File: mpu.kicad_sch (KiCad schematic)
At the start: 31 parts, among them SW501 SW_DIP_x03, U501 STM32MP135FAE7, Y501 32.768 kHz, Y502 24 MHz

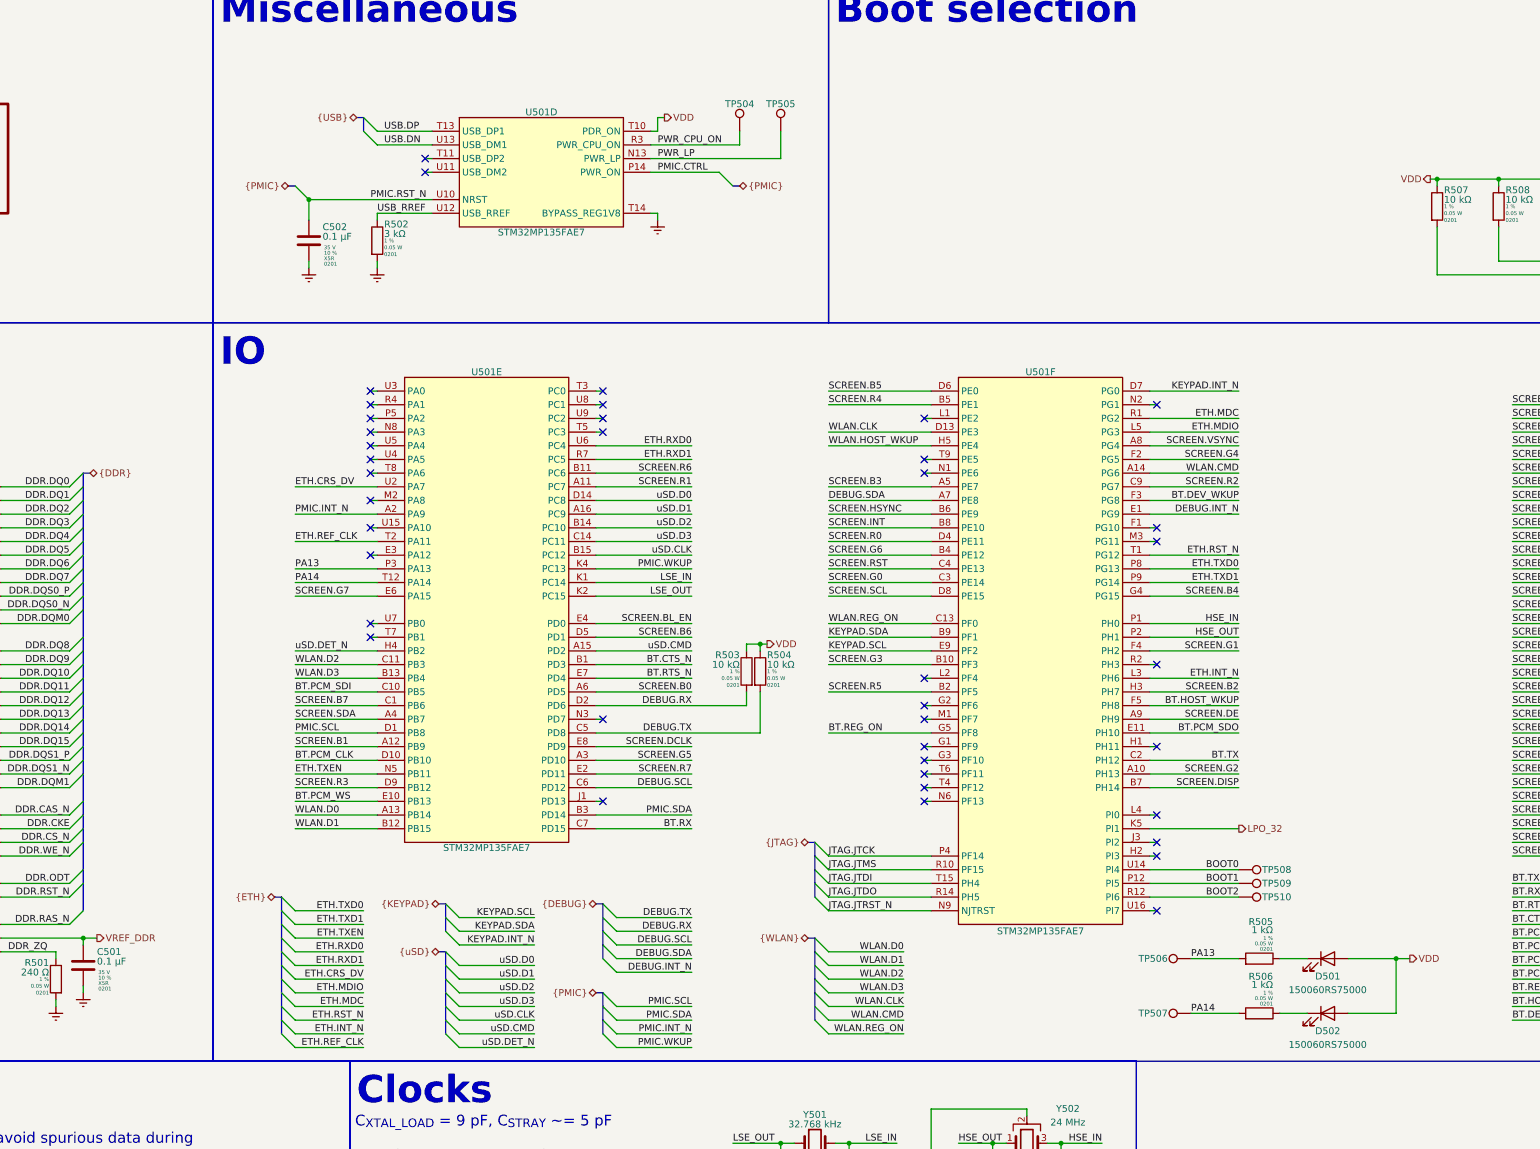
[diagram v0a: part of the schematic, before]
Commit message: Fix PMIC symbol and MPU labels
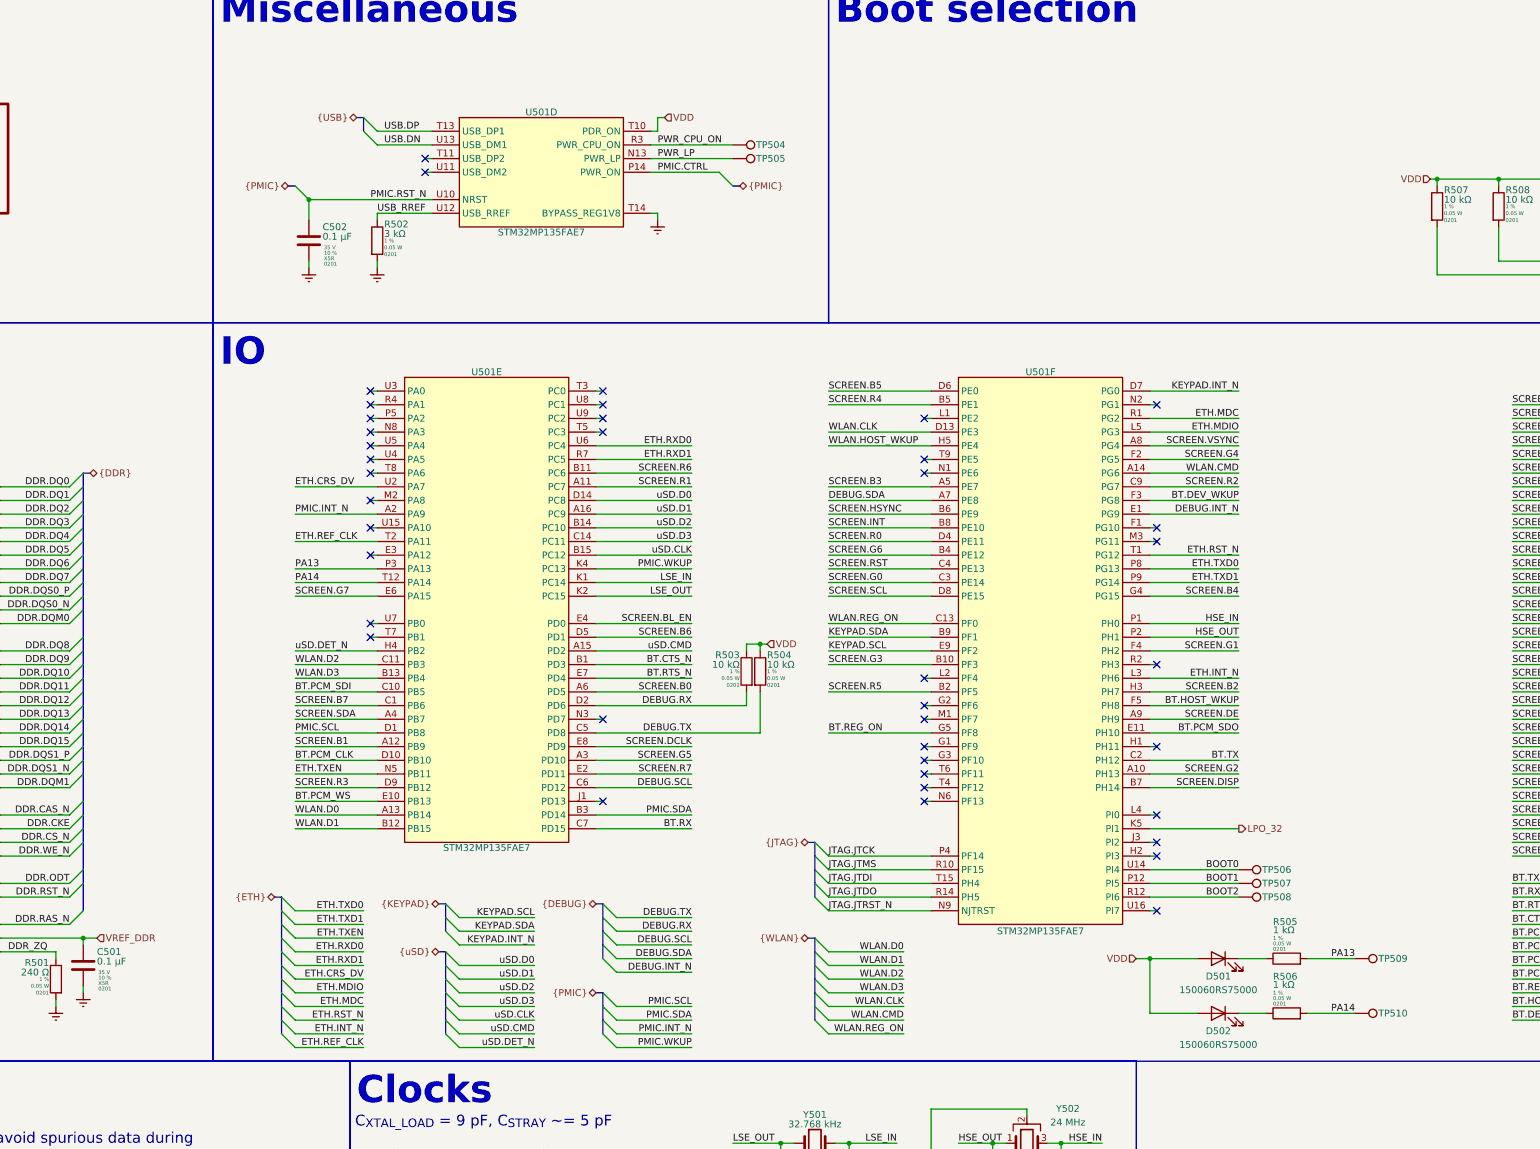
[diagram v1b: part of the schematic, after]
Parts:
- renumbered TP508 to TP506, TP509 to TP507, TP510 to TP508, TP506 to TP509, TP507 to TP510
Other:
- moved on the sheet: D501, D502, R505, R506, TP509, TP510

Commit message: Fix symbols and footprint assignments
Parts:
- SW501: footprint Package_DIP:DIP-6_W7.62mm -> Button_Switch_THT:SW_DIP_SPSTx03_Slide_9.78x9.8mm_W7.62mm_P2.54mm; symbol Switch:SW_DIP_x03 -> linux-sbc:SW_DIP_x03
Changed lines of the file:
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@@
 	)
 	(symbol
-		(lib_id "Switch:SW_DIP_x03")
+		(lib_id "linux-sbc:SW_DIP_x03")
 		(at 392.43 102.87 0)
 		(unit 1)
@@
 			)
 		)
-		(property "Footprint" "Package_DIP:DIP-6_W7.62mm"
+		(property "Footprint" "Button_Switch_THT:SW_DIP_SPSTx03_Slide_9.78x9.8mm_W7.62mm_P2.54mm"
 			(at 392.43 105.41 0)
 			(effects
@@
 			)
 		)
-		(property "Datasheet" "https://www.cuidevices.com/product/resource/ds01-254.pdf"
+		(property "Datasheet" "~"
 			(at 392.43 105.41 0)
 			(effects
@@
 			)
 		)
-		(property "Description" "Dip Switch SPST 3 Position Through Hole Slide (Standard) Actuator 25mA 24VDC"
+		(property "Description" "3x DIP Switch, Single Pole Single Throw (SPST) switch, small symbol"
 			(at 392.43 102.87 0)
 			(effects

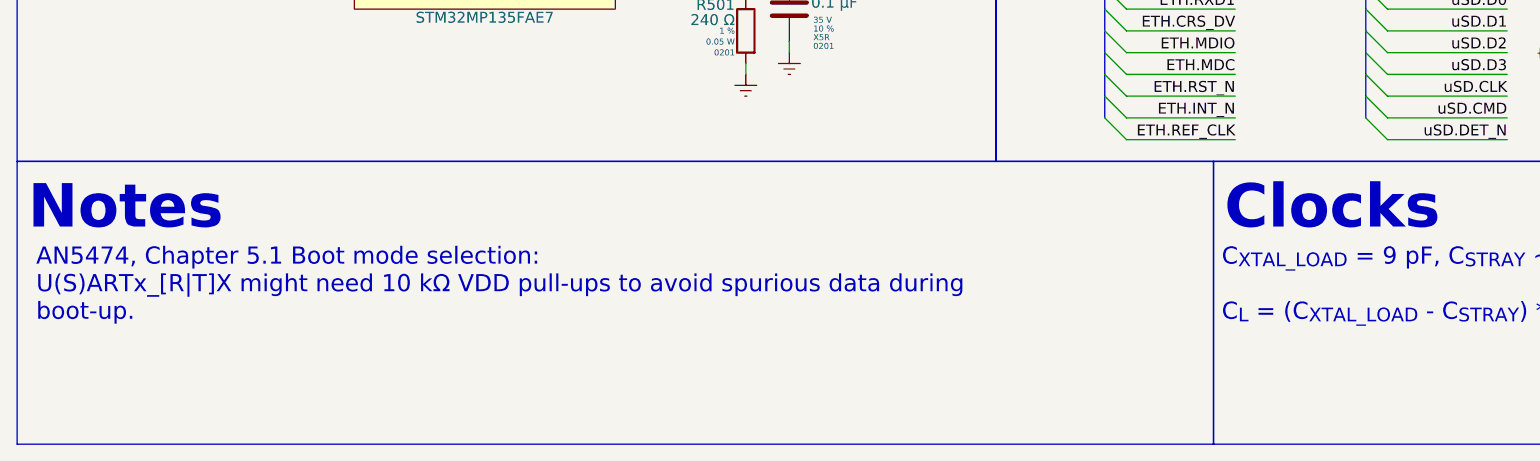
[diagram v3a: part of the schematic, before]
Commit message: Refactor text with ChatGPT and make schematics more readable
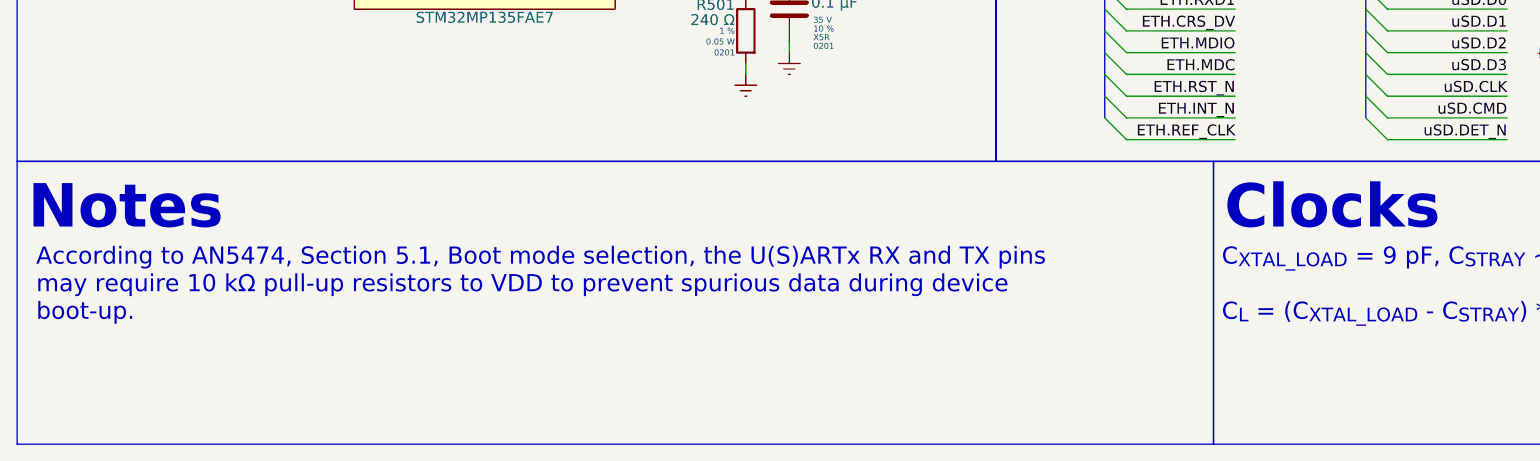
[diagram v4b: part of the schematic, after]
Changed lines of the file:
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@@
 		)
 	)
-	(text_box "AN5474, Chapter 5.1 Boot mode selection:\nU(S)ARTx_[R|T]X might need 10 kΩ VDD pull-ups to avoid spurious data during boot-up."
+	(text_box "According to AN5474, Section 5.1, Boot mode selection, the U(S)ARTx RX and TX pins may require 10 kΩ pull-up resistors to VDD to prevent spurious data during device boot-up."
 		(exclude_from_sim no)
 		(at 13.97 260.35 0)

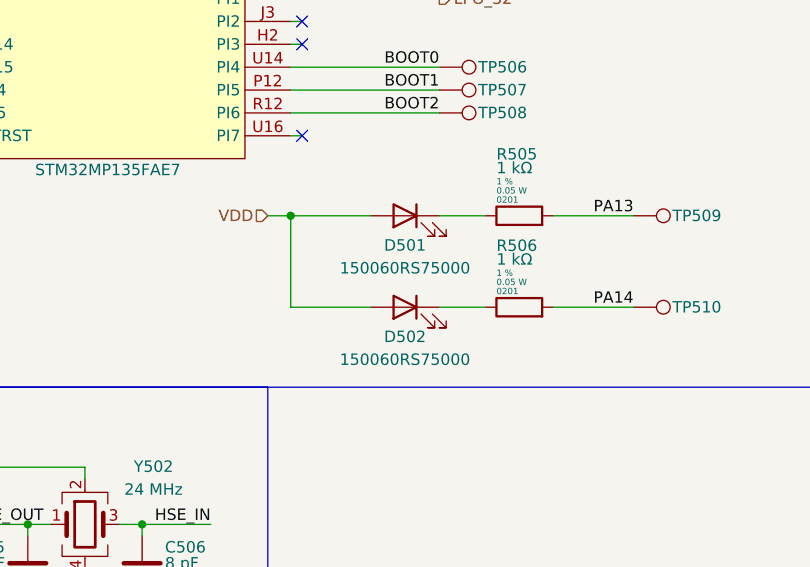
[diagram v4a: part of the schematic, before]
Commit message: Rework Red LED BOM and info, rework debug USB-to-UART
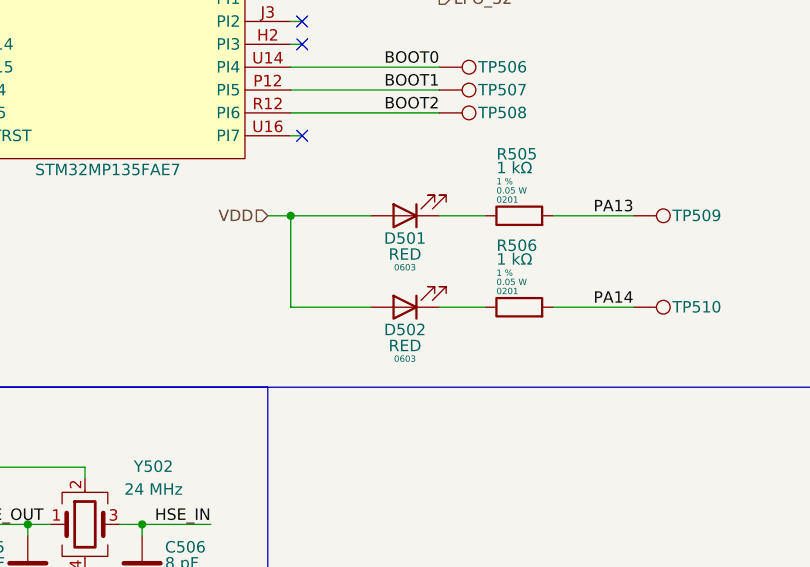
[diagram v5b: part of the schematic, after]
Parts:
- D501, D502: value 150060RS75000 -> RED; Size (none) -> 0603
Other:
- moved on the sheet: D501
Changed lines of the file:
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@@
 			)
 		)
-		(property "Datasheet" "~"
+		(property "Datasheet" "https://www.cuidevices.com/product/resource/ds01-254.pdf"
 			(at 392.43 105.41 0)
 			(effects
@@
 	)
 	(symbol
+		(lib_name "LED_1")
 		(lib_id "Device:LED")
-		(at 313.69 232.41 0)
-		(mirror y)
+		(at 313.69 232.41 180)
 		(unit 1)
 		(exclude_from_sim no)
@@
 		(dnp no)
 		(property "Reference" "D501"
-			(at 313.69 234.95 0)
+			(at 313.69 234.188 0)
 			(effects
 				(font
 					(size 1.27 1.27)
 				)
-				(justify top)
+				(justify bottom)
 			)
 		)
-		(property "Value" "150060RS75000"
-			(at 313.69 237.49 0)
+		(property "Value" "RED"
+			(at 313.69 235.966 0)
 			(effects
 				(font
 					(size 1.27 1.27)
 				)
-				(justify top)
+				(justify bottom)
 			)
 		)
@@
 			)
 		)
+		(property "Size" "0603"
+			(at 313.69 237.744 0)
+			(effects
+				(font
+					(size 0.7 0.7)
+				)
+				(justify bottom)
+			)
+		)
 		(pin "2"
 		)
@@
 	)
 	(symbol
-		(lib_id "Device:LED")
-		(at 313.69 242.57 0)
-		(mirror y)
-		(unit 1)
-		(exclude_from_sim no)
-		(in_bom yes)
-		(on_board yes)
-		(dnp no)
-		(property "Reference" "D502"
-			(at 313.69 245.11 0)
-			(effects
-				(font
-					(size 1.27 1.27)
-				)
-				(justify top)
-			)
-		)
-		(property "Value" "150060RS75000"
-			(at 313.69 247.65 0)
-			(effects
-				(font
-					(size 1.27 1.27)
-				)
-				(justify top)
-			)
-		)
-		(property "Footprint" "LED_SMD:LED_0603_1608Metric"
-			(at 313.69 242.57 0)
-			(effects
-				(font
-					(size 1.27 1.27)
-				)
-				(hide yes)
-			)
-		)
-		(property "Datasheet" "https://www.we-online.com/components/products/datasheet/150060RS75000.pdf"
-			(at 313.69 242.57 0)
-			(effects
-				(font
-					(size 1.27 1.27)
-				)
-				(hide yes)
-			)
-		)
-		(property "Description" "Red 625nm LED Indication - Discrete 2V 0603 (1608 Metric)"
-			(at 313.69 242.57 0)
-			(effects
-				(font
-					(size 1.27 1.27)
-				)
-				(hide yes)
-			)
-		)
-		(property "MPN" "150060RS75000"
-			(at 313.69 242.57 0)
-			(effects
-				(font
-					(size 1.27 1.27)
-				)
-				(hide yes)
-			)
-		)
-		(property "Manufacturer" "Würth Elektronik"
-			(at 313.69 242.57 0)
-			(effects
-				(font
-					(size 1.27 1.27)
-				)
-				(hide yes)
-			)
-		)
-		(property "Digi-Key Part Number" "732-4978-1-ND"
-			(at 313.69 242.57 0)
-			(effects
-				(font
-					(size 1.27 1.27)
-				)
-				(hide yes)
-			)
-		)
-		(pin "2"
-		)
-		(pin "1"
-		)
-		(instances
-			(project "linux-sbc"
-				(path "/fa11a02f-8043-4153-ab69-88d766503017/2d01087b-54dc-4f43-9cc7-a0ba17201776"
-					(reference "D502")
-					(unit 1)
-				)
-			)
-		)
-	)
-	(symbol
 		(lib_id "power:Earth")
 		(at 284.48 279.4 0)
@@
 					(unit 1)
 				)
+			)
+		)
+	)
+	(symbol
+		(lib_name "LED_1")
+		(lib_id "Device:LED")
+		(at 313.69 242.57 180)
+		(unit 1)
+		(exclude_from_sim no)
+		(in_bom yes)
+		(on_board yes)
+		(dnp no)
+		(property "Reference" "D502"
+			(at 313.69 244.348 0)
+			(effects
+				(font
+					(size 1.27 1.27)
+				)
+				(justify bottom)
+			)
+		)
+		(property "Value" "RED"
+			(at 313.69 246.126 0)
+			(effects
+				(font
+					(size 1.27 1.27)
+				)
+				(justify bottom)
+			)
+		)
+		(property "Footprint" "LED_SMD:LED_0603_1608Metric"
+			(at 313.69 242.57 0)
+			(effects
+				(font
+					(size 1.27 1.27)
+				)
+				(hide yes)
+			)
+		)
+		(property "Datasheet" "https://www.we-online.com/components/products/datasheet/150060RS75000.pdf"
+			(at 313.69 242.57 0)
+			(effects
+				(font
+					(size 1.27 1.27)
+				)
+				(hide yes)
+			)
+		)
+		(property "Description" "Red 625nm LED Indication - Discrete 2V 0603 (1608 Metric)"
+			(at 313.69 242.57 0)
+			(effects
+				(font
+					(size 1.27 1.27)
+				)
+				(hide yes)
+			)
+		)
+		(property "MPN" "150060RS75000"
+			(at 313.69 242.57 0)
+			(effects
+				(font
+					(size 1.27 1.27)
+				)
+				(hide yes)
+			)
+		)
+		(property "Manufacturer" "Würth Elektronik"
+			(at 313.69 242.57 0)
+			(effects
+				(font
+					(size 1.27 1.27)
+				)
+				(hide yes)
+			)
+		)
+		(property "Digi-Key Part Number" "732-4978-1-ND"
+			(at 313.69 242.57 0)
+			(effects
+				(font
+					(size 1.27 1.27)
+				)
+				(hide yes)
+			)
+		)
+		(property "Size" "0603"
+			(at 313.69 247.904 0)
+			(effects
+				(font
+					(size 0.7 0.7)
+				)
+				(justify bottom)
+			)
+		)
+		(pin "2"
+		)
+		(pin "1"
+		)
+		(instances
+			(project "linux-sbc"
+				(path "/fa11a02f-8043-4153-ab69-88d766503017/2d01087b-54dc-4f43-9cc7-a0ba17201776"
+					(reference "D502")
+					(unit 1)
+				)
